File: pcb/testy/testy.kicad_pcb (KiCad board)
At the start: 2 copper layers, 114.5 x 101.4 mm, 100 parts, among them J1 L_XLED, J2 R_XLED, J3 SLAVE_LED, P1 OLED, P2 ICSP, SW0:0 SW_Push, SW0:1 SW_Push, SW0:2 SW_Push, SW0:3 SW_Push, SW0:4 SW_Push, SW1:0 SW_Push, SW1:1 SW_Push, SW1:2 SW_Push, SW1:3 SW_Push, SW1:4 SW_Push, SW2:0 SW_Push, SW2:1 SW_Push, SW2:2 SW_Push, SW2:3 SW_Push, SW2:4 SW_Push, SW3:0 SW_Push, SW3:1 SW_Push, SW3:2 SW_Push, SW3:3 SW_Push, SW3:4 SW_Push, SW3:5 SW_Push, SW4:1 SW_Push, SW4:2 SW_Push, SW4:3 SW_Push, SW4:4 SW_Push, SW4:5 SW_Push

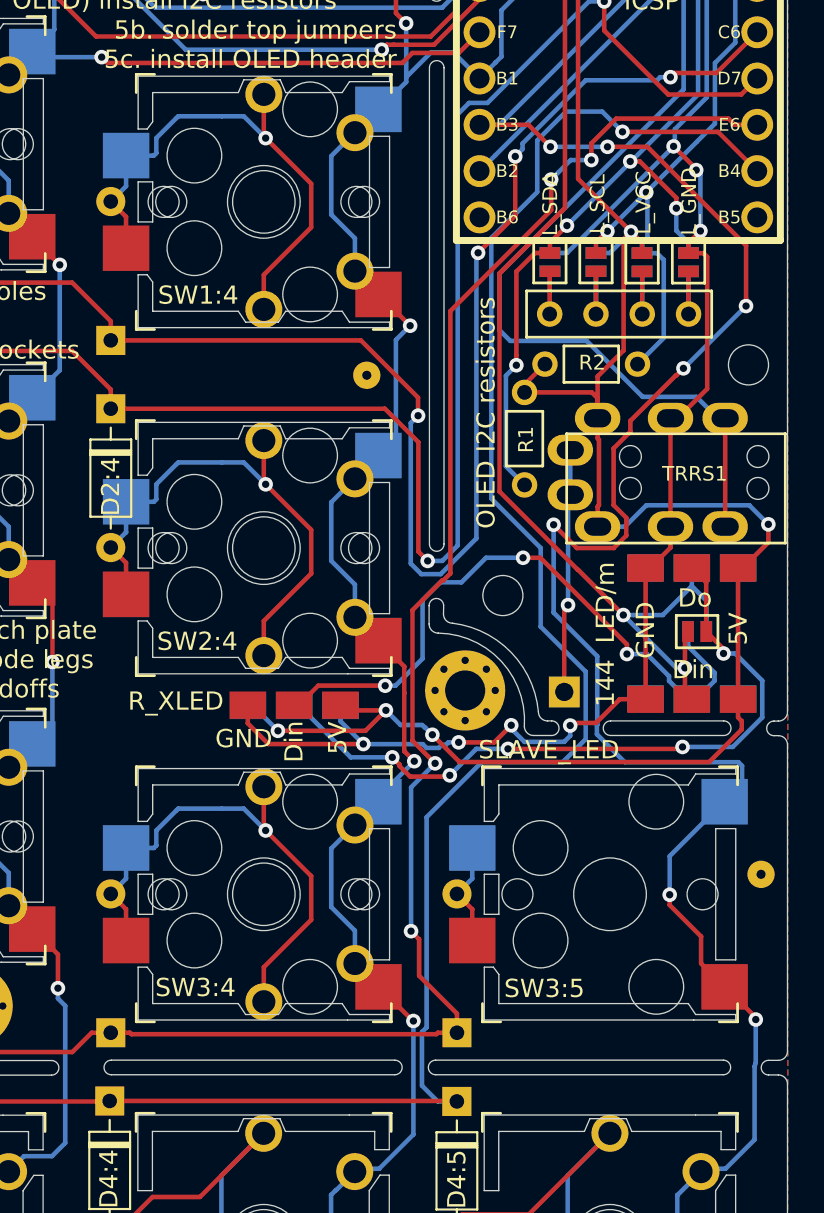
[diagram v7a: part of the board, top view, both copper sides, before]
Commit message: feat: add back LED bypass jumpers
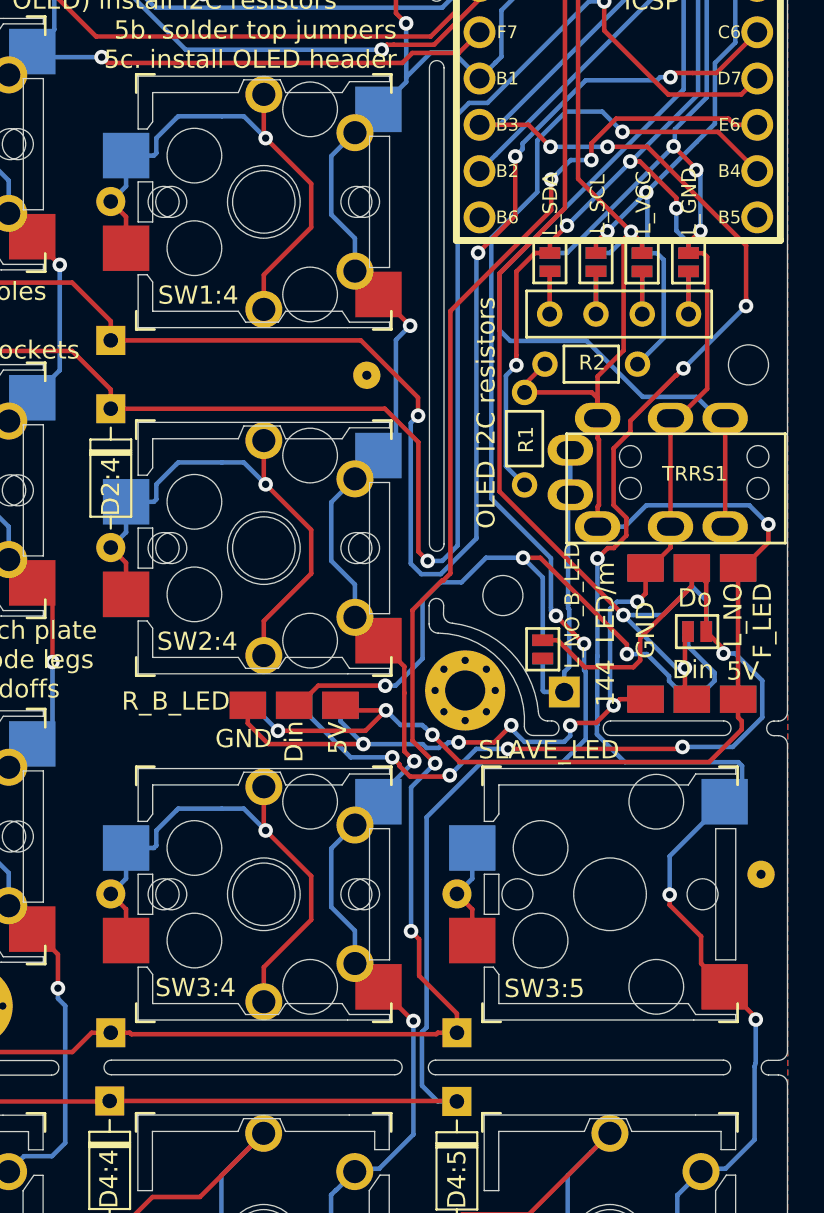
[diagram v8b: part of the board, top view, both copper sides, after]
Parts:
- added JP10: L_NO_B_LED, footprints:Jumper, F.Cu at (173.5, 103.3)
- added JP11: R_NO_B_LED, footprints:Jumper, B.Cu at (173.5, 103.3)
- J1: value L_XLED -> L_B_LED
- J2: value R_XLED -> R_B_LED
- JP12: value R_NOLED -> R_NO_F_LED
- JP9: value L_NOLED -> L_NO_F_LED
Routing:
- net Net-(J1-Pad2): track 38.9 -> 51.2 mm
- net Col5: track 112.9 -> 107.4 mm
- net Net-(J2-Pad2): track 35.7 -> 40.7 mm
- net SLAVE_LED: track 13.4 -> 16.4 mm, vias 1 -> 0
- net GND: track 249.4 -> 251.2 mm, vias 8 -> 10
- net Row4: vias 1 -> 3
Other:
- board text added: "L_NO F_LED"
- board text added: "R_NO F_LED"
